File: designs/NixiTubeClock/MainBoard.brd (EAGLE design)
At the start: 98 x 67 mm, 45 parts, among them IC1 LD117ADT-TR, J1 S2B-NSHSS-TB, J2 S2B-NSHSS-TB, J3 S2B-NSHSS-TB, J4 PJ-002AH-SMT-TR, J5 S2B-NSHSS-TB, Q1 2N7002NXAKR, Q2 2N7002NXAKR

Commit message: added new cam data and made last checks before order :o
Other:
- board text added: "°C/%"
- board text removed: "T/H"
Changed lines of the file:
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@@
 <setting verticaltext="up"/>
 </settings>
-<grid distance="0.5" unitdist="mm" unit="mm" style="lines" multiple="1" display="yes" altdistance="5" altunitdist="mil" altunit="mil"/>
+<grid distance="1" unitdist="mm" unit="mm" style="lines" multiple="1" display="yes" altdistance="5" altunitdist="mil" altunit="mil"/>
 <layers>
 <layer number="1" name="Top" color="4" fill="1" visible="yes" active="yes"/>
@@
 </layers>
 <board>
-<fusionsync huburn="a.cGVyc29uYWw6dWUyYTNmMDU1" projecturn="a.cGVyc29uYWw6dWUyYTNmMDU1IzIwMTgxMjEwMTY0OTQ5MjI2" f3durn="urn:adsk.wipprod:dm.lineage:sIc1WYWiRnKTMBUjB1WWbw" pcbguid="963d08c0-42bd-4bef-8ac7-da9e1254c3c3" lastpulledtime="" lastsyncedchangeguid="29938a95-c5d6-387e-86ed-b41e76510cf1"/>
+<fusionsync huburn="a.cGVyc29uYWw6dWUyYTNmMDU1" projecturn="a.cGVyc29uYWw6dWUyYTNmMDU1IzIwMTgxMjEwMTY0OTQ5MjI2" f3durn="urn:adsk.wipprod:dm.lineage:sIc1WYWiRnKTMBUjB1WWbw" pcbguid="963d08c0-42bd-4bef-8ac7-da9e1254c3c3" lastpulledtime="" lastsyncedchangeguid="06c0c3c6-15d9-9501-93bf-f9a5b0f67d39"/>
 <plain>
 <hole x="3" y="50" drill="2.8"/>
@@
 <text x="83.02945" y="8.5" size="1.016" layer="25" rot="R90">GND</text>
 <text x="81.47055" y="8.5" size="1.016" layer="25" rot="R90">3.3V</text>
-<text x="64.47055" y="8.5" size="1.016" layer="25" rot="R90">GND</text>
-<text x="65.97055" y="8.5" size="1.016" layer="25" rot="R90">RXD0</text>
+<text x="65.97055" y="8.5" size="1.016" layer="25" rot="R90">GND</text>
+<text x="67.47055" y="8.5" size="1.016" layer="25" rot="R90">RXD0</text>
 <rectangle x1="-10.16048125" y1="33.39915" x2="-10.15031875" y2="33.41185" layer="1" rot="R270"/>
 <wire x1="0" y1="53" x2="10" y2="63" width="0.127" layer="20" curve="-90"/>
@@
 <text x="18.5" y="32" size="1.778" layer="25">3.3V</text>
 <text x="2.5" y="29" size="1.778" layer="25" rot="R270">RTC</text>
-<text x="37.3" y="4.4" size="1.778" layer="25">T/H</text>
+<text x="31.8" y="5.4" size="1.778" layer="25">°C/%</text>
 <text x="60" y="38" size="1.778" layer="25">180V</text>
-<text x="45.5" y="5" size="1.778" layer="25">NIXIs</text>
+<text x="44.5" y="5.5" size="1.778" layer="25">NIXIs</text>
 <text x="40" y="46.5" size="1.778" layer="25">ESP32</text>
-<text x="34.1" y="4.67055" size="1.016" layer="26" rot="R90">GND</text>
-<text x="36.7" y="4.67055" size="1.016" layer="26" rot="R90">3.3V</text>
+<text x="34.1" y="5.17055" size="1.016" layer="26" rot="R90">GND</text>
+<text x="36.7" y="5.17055" size="1.016" layer="26" rot="R90">3.3V</text>
 </plain>
 <attributes>

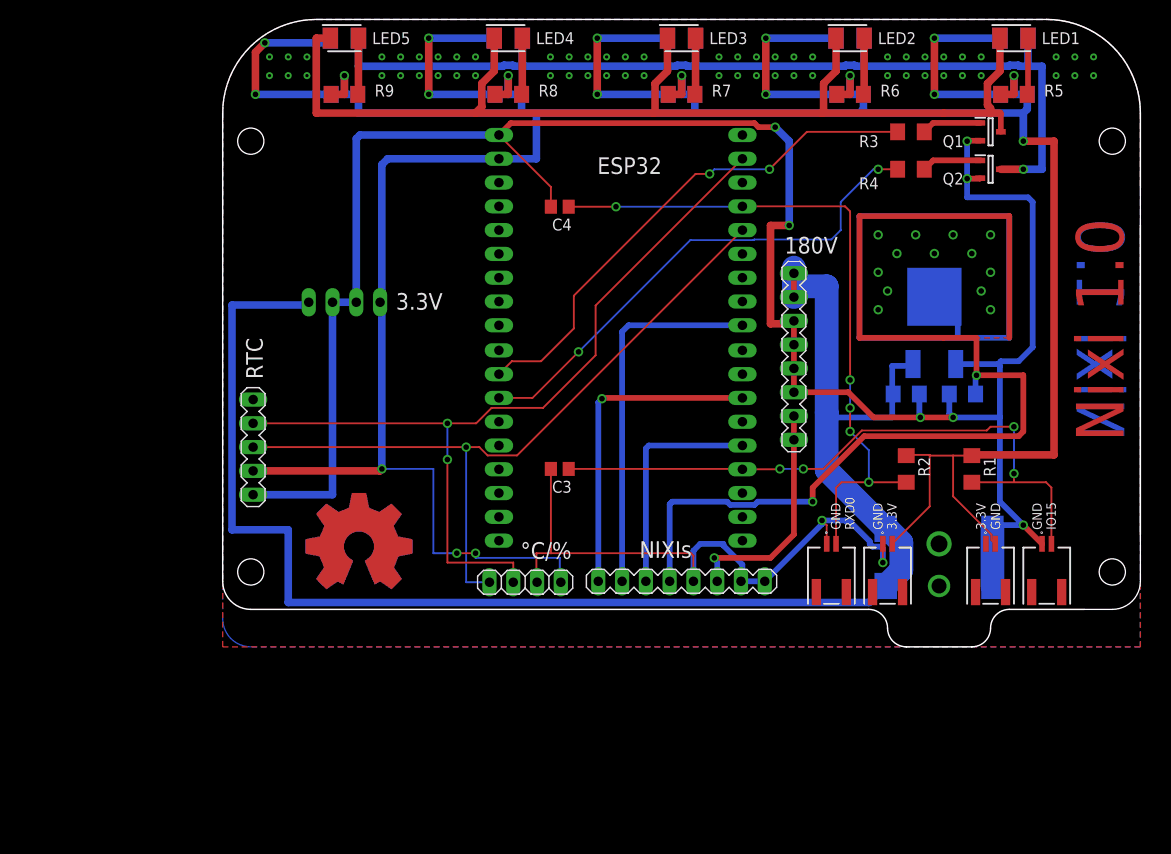
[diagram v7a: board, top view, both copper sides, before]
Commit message: added first IN-4 Design and edited mainboard to fit all screws for IN-4
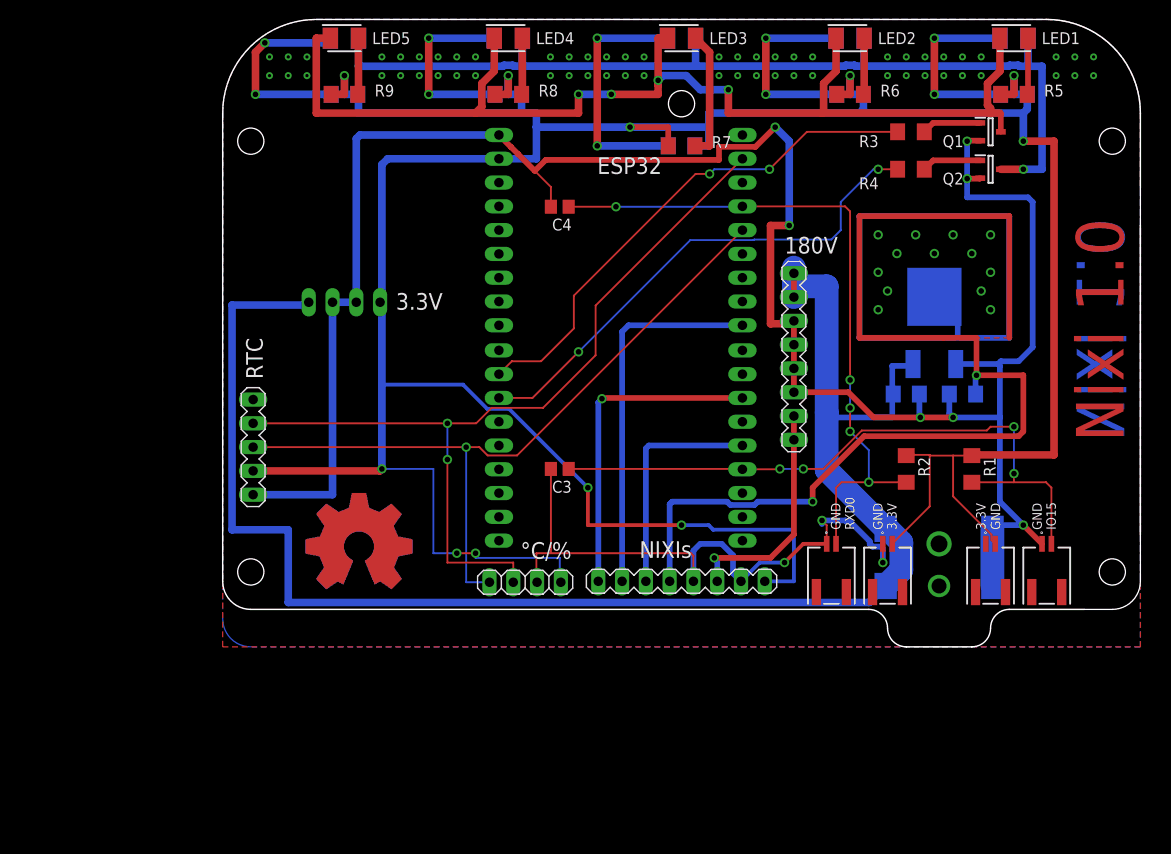
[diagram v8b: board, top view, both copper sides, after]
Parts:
- moved R12 5.50 mm to (49.0, 49.5)
- moved R7 5.50 mm to (49.0, 49.5)
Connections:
- net 3.3V: now also SV1.8
- net GND: no longer SV1.8
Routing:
- net 3.3V: track 293.2 -> 356.8 mm, vias 9 -> 11
- net N$4: track 6.03 -> 13.7 mm
- net N$12: track 21.1 -> 26.6 mm
- net N$28: track 119.3 -> 123.0 mm, vias 0 -> 4
- net GND: track 312.5 -> 315.6 mm, vias 9 -> 10
